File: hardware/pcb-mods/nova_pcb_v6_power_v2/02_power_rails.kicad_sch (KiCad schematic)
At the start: 12 parts, among them J12 XT30_JET_12V, J13 XT30_L2_12V, J2 UBEC_5V_AUX, U1 Pololu_D42V110F7_LEG_7V5, U2 Pololu_D42V110F12_HIP_12V, U3 Pololu_D24V22F12_L2_12V, U4 Pololu_D42V55F12_JET_12V, U5 Pololu_D42V55F7_ARM_7V5

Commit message: pcb(v6-power-v2): backfill MPN + Manufacturer fields — 100% BOM coverage
All 50 BOM components now carry MPNs from the verified order list:
Yageo RC0603 resistor set (R14 470k = Vishay CRCW0603 DigiKey sub),
Nichicon UPW1E bulk caps, Bourns SRR1260-220M, Infineon IRLB3034PBF,
onsemi BSS138 x3, TI LM393DR, Pololu buck modules (off-board),
GODIY INA226 20A R002 modules with I2C addresses in Manufacturer field,
AMASS XT60H/XT30U, JST B3B-XH-A, Adam Tech BHR-12-VUA, Sullins headers.
ERC: 0 errors (1 expected V7V5_ARM warning). kicad-happy bom_lock: pass.

Co-Authored-By: Claude Fable 5 <noreply@anthropic.com>
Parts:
- C6, C8, C9: MPN (none) -> UPW1E471MPD; Manufacturer (none) -> Nichicon
- J12, J13: MPN (none) -> XT30U-M; Manufacturer (none) -> AMASS
- J2: MPN (none) -> PRPC040SAAN-RC; Manufacturer (none) -> Sullins (snap to 1x03)
- L1: MPN (none) -> SRR1260-220M; Manufacturer (none) -> Bourns
- U1: MPN (none) -> D42V110F7; Manufacturer (none) -> Pololu (#5674, off-board module)
- U2: MPN (none) -> D42V110F12; Manufacturer (none) -> Pololu (#5677, off-board module)
- U3: MPN (none) -> D24V22F12; Manufacturer (none) -> Pololu (#2855, off-board module)
- U4: MPN (none) -> D42V55F12; Manufacturer (none) -> Pololu (#5577, off-board module)
- U5: MPN (none) -> D42V55F7; Manufacturer (none) -> Pololu (Phase 4 reserve, DNP)
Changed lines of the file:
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@@
+			)
+		)
+		(property "Manufacturer" "Pololu (#5577, off-board module)" (at 0 0 0)
+			(effects
+				(font
+					(size 1.27 1.27)
+				)
+				(hide yes)
+			)
+		)
+		(property "MPN" "D42V55F12" (at 0 0 0)
+			(effects
+				(font
+					(size 1.27 1.27)
+				)
+				(hide yes)
 			)
 		)
@@
 			)
 		)
+		(property "Manufacturer" "Sullins (snap to 1x03)" (at 0 0 0)
+			(effects
+				(font
+					(size 1.27 1.27)
+				)
+				(hide yes)
+			)
+		)
+		(property "MPN" "PRPC040SAAN-RC" (at 0 0 0)
+			(effects
+				(font
+					(size 1.27 1.27)
+				)
+				(hide yes)
+			)
+		)
 		(pin "1"
 		)
@@
 					(size 1.27 1.27)
 				)
+			)
+		)
+		(property "Manufacturer" "Pololu (#5674, off-board module)" (at 0 0 0)
+			(effects
+				(font
+					(size 1.27 1.27)
+				)
+				(hide yes)
+			)
+		)
+		(property "MPN" "D42V110F7" (at 0 0 0)
+			(effects
+				(font
+					(size 1.27 1.27)
+				)
+				(hide yes)
 			)
 		)
@@
 			)
 		)
+		(property "Manufacturer" "Pololu (Phase 4 reserve, DNP)" (at 0 0 0)
+			(effects
+				(font
+					(size 1.27 1.27)
+				)
+				(hide yes)
+			)
+		)
+		(property "MPN" "D42V55F7" (at 0 0 0)
+			(effects
+				(font
+					(size 1.27 1.27)
+				)
+				(hide yes)
+			)
+		)
 		(pin "1"
 		)
@@
 			)
 		)
+		(property "Manufacturer" "Pololu (#5677, off-board module)" (at 0 0 0)
+			(effects
+				(font
+					(size 1.27 1.27)
+				)
+				(hide yes)
+			)
+		)
+		(property "MPN" "D42V110F12" (at 0 0 0)
+			(effects
+				(font
+					(size 1.27 1.27)
+				)
+				(hide yes)
+			)
+		)
 		(pin "1"
 		)
@@
 			)
 		)
+		(property "Manufacturer" "Pololu (#2855, off-board module)" (at 0 0 0)
+			(effects
+				(font
+					(size 1.27 1.27)
+				)
+				(hide yes)
+			)
+		)
+		(property "MPN" "D24V22F12" (at 0 0 0)
+			(effects
+				(font
+					(size 1.27 1.27)
+				)
+				(hide yes)
+			)
+		)
 		(pin "1"
 		)
@@
 		(property "Datasheet" "~"
 			(at 129.54 105.41 0)
+			(effects
+				(font
+					(size 1.27 1.27)
+				)
+				(hide yes)
+			)
+		)
+		(property "Manufacturer" "AMASS" (at 0 0 0)
+			(effects
+				(font
+					(size 1.27 1.27)
+				)
+				(hide yes)
+			)
+		)
+		(property "MPN" "XT30U-M" (at 0 0 0)
 			(effects
 				(font
@@
 			)
 		)
+		(property "Manufacturer" "AMASS" (at 0 0 0)
+			(effects
+				(font
+					(size 1.27 1.27)
+				)
+				(hide yes)
+			)
+		)
+		(property "MPN" "XT30U-M" (at 0 0 0)
+			(effects
+				(font
+					(size 1.27 1.27)
+				)
+				(hide yes)
+			)
+		)
 		(pin "1"
 		)
@@
 			)
 		)
+		(property "Manufacturer" "Bourns" (at 0 0 0)
+			(effects
+				(font
+					(size 1.27 1.27)
+				)
+				(hide yes)
+			)
+		)
+		(property "MPN" "SRR1260-220M" (at 0 0 0)
+			(effects
+				(font
+					(size 1.27 1.27)
+				)
+				(hide yes)
+			)
+		)
 		(pin "1"
 		)
@@
 			)
 		)
+		(property "Manufacturer" "Nichicon" (at 0 0 0)
+			(effects
+				(font
+					(size 1.27 1.27)
+				)
+				(hide yes)
+			)
+		)
+		(property "MPN" "UPW1E471MPD" (at 0 0 0)
+			(effects
+				(font
+					(size 1.27 1.27)
+				)
+				(hide yes)
+			)
+		)
 		(pin "1"
 		)
@@
 			)
 		)
+		(property "Manufacturer" "Nichicon" (at 0 0 0)
+			(effects
+				(font
+					(size 1.27 1.27)
+				)
+				(hide yes)
+			)
+		)
+		(property "MPN" "UPW1E471MPD" (at 0 0 0)
+			(effects
+				(font
+					(size 1.27 1.27)
+				)
+				(hide yes)
+			)
+		)
 		(pin "1"
 		)
@@
 			(effects
 				(font
+					(size 1.27 1.27)
+				)
+				(hide yes)
+			)
+		)
+		(property "Manufacturer" "Nichicon" (at 0 0 0)
+			(effects
+				(font
+					(size 1.27 1.27)
+				)
+				(hide yes)
+			)
+		)
+		(property "MPN" "UPW1E471MPD" (at 0 0 0)
+			(effects
+				(font

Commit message: pcb(v6-power-v2): correct C1-C5 to FymuSing (as purchased) + DigiKey PNs from order CSV
Verified against Complete_Digikey_Order_NOVA.csv (16 lines, all match):
R14 470k confirmed Vishay CRCW0603470KFKEA (541-470KHCT-ND).
C1-C5 corrected Nichicon->FymuSing 1000uF/25V (Amazon purchase, 10x17mm).
Remaining 23 parts without DigiKey PN are Amazon/Pololu/AMASS sourced.

Co-Authored-By: Claude Fable 5 <noreply@anthropic.com>
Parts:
- C6, C8, C9: DigiKey (none) -> 493-1826-ND
- J2: DigiKey (none) -> S1011EC-40-ND
- L1: DigiKey (none) -> SRR1260-220MCT-ND
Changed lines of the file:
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@@
+			)
+		)
+		(property "DigiKey" "S1011EC-40-ND" (at 0 0 0)
+			(effects
+				(font
+					(size 1.27 1.27)
+				)
+				(hide yes)
 			)
 		)
@@
 			)
 		)
+		(property "DigiKey" "SRR1260-220MCT-ND" (at 0 0 0)
+			(effects
+				(font
+					(size 1.27 1.27)
+				)
+				(hide yes)
+			)
+		)
 		(pin "1"
 		)
@@
 			)
 		)
+		(property "DigiKey" "493-1826-ND" (at 0 0 0)
+			(effects
+				(font
+					(size 1.27 1.27)
+				)
+				(hide yes)
+			)
+		)
 		(pin "1"
 		)
@@
 			)
 		)
+		(property "DigiKey" "493-1826-ND" (at 0 0 0)
+			(effects
+				(font
+					(size 1.27 1.27)
+				)
+				(hide yes)
+			)
+		)
 		(pin "1"
 		)
@@
 			(effects
 				(font
+					(size 1.27 1.27)
+				)
+				(hide yes)
+			)
+		)
+		(property "DigiKey" "493-1826-ND" (at 0 0 0)
+			(effects
+				(font

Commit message: pcb(v6-power-v2): AssemblyOrder fields + assembly-sequenced iBOM
15-step hand-solder sequence (flat->tall, SMD bottom cluster -> THT top):
0603s -> SOT-23 -> SOIC -> L1 -> INA headers -> headers/JST/IDC ->
screw blocks -> XT30 -> XT60 -> Q1 (Step 10a test first) -> 470uF -> 1000uF.
bom/ibom_assembly.html groups by AssemblyOrder via netlist extra-data.

Co-Authored-By: Claude Fable 5 <noreply@anthropic.com>
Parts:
- C6, C8, C9: AssemblyOrder (none) -> 14 THT 470uF
- J12, J13: AssemblyOrder (none) -> 11 THT XT30
- J2: AssemblyOrder (none) -> 07 THT pin header
- L1: AssemblyOrder (none) -> 05 SMD inductor (big pads, max iron heat)
- U1, U2, U3, U4: AssemblyOrder (none) -> 11 THT XT30 (buck landing)
- U5: AssemblyOrder (none) -> 11 THT XT30 (buck landing, DNP option)
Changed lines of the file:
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@@
+			)
+		)
+		(property "AssemblyOrder" "11 THT XT30 (buck landing)" (at 0 0 0)
+			(effects
+				(font
+					(size 1.27 1.27)
+				)
+				(hide yes)
 			)
 		)
@@
 			)
 		)
+		(property "AssemblyOrder" "07 THT pin header" (at 0 0 0)
+			(effects
+				(font
+					(size 1.27 1.27)
+				)
+				(hide yes)
+			)
+		)
 		(pin "1"
 		)
@@
 		)
 		(property "MPN" "D42V110F7" (at 0 0 0)
+			(effects
+				(font
+					(size 1.27 1.27)
+				)
+				(hide yes)
+			)
+		)
+		(property "AssemblyOrder" "11 THT XT30 (buck landing)" (at 0 0 0)
 			(effects
 				(font
@@
 			)
 		)
+		(property "AssemblyOrder" "11 THT XT30 (buck landing, DNP option)" (at 0 0 0)
+			(effects
+				(font
+					(size 1.27 1.27)
+				)
+				(hide yes)
+			)
+		)
 		(pin "1"
 		)
@@
 			)
 		)
+		(property "AssemblyOrder" "11 THT XT30 (buck landing)" (at 0 0 0)
+			(effects
+				(font
+					(size 1.27 1.27)
+				)
+				(hide yes)
+			)
+		)
 		(pin "1"
 		)
@@
 			)
 		)
+		(property "AssemblyOrder" "11 THT XT30 (buck landing)" (at 0 0 0)
+			(effects
+				(font
+					(size 1.27 1.27)
+				)
+				(hide yes)
+			)
+		)
 		(pin "1"
 		)
@@
 		)
 		(property "MPN" "XT30U-M" (at 0 0 0)
+			(effects
+				(font
+					(size 1.27 1.27)
+				)
+				(hide yes)
+			)
+		)
+		(property "AssemblyOrder" "11 THT XT30" (at 0 0 0)
 			(effects
 				(font
@@
 			)
 		)
+		(property "AssemblyOrder" "11 THT XT30" (at 0 0 0)
+			(effects
+				(font
+					(size 1.27 1.27)
+				)
+				(hide yes)
+			)
+		)
 		(pin "1"
 		)
@@
 			)
 		)
+		(property "AssemblyOrder" "05 SMD inductor (big pads, max iron heat)" (at 0 0 0)
+			(effects
+				(font
+					(size 1.27 1.27)
+				)
+				(hide yes)
+			)
+		)
 		(pin "1"
 		)
@@
 			)
 		)
+		(property "AssemblyOrder" "14 THT 470uF" (at 0 0 0)
+			(effects
+				(font
+					(size 1.27 1.27)
+				)
+				(hide yes)
+			)
+		)
 		(pin "1"
 		)
@@
 			)
 		)
+		(property "AssemblyOrder" "14 THT 470uF" (at 0 0 0)
+			(effects
+				(font
+					(size 1.27 1.27)
+				)
+				(hide yes)
+			)
+		)
 		(pin "1"
 		)
@@
 			(effects
 				(font
+					(size 1.27 1.27)
+				)
+				(hide yes)
+			)
+		)
+		(property "AssemblyOrder" "14 THT 470uF" (at 0 0 0)
+			(effects
+				(font

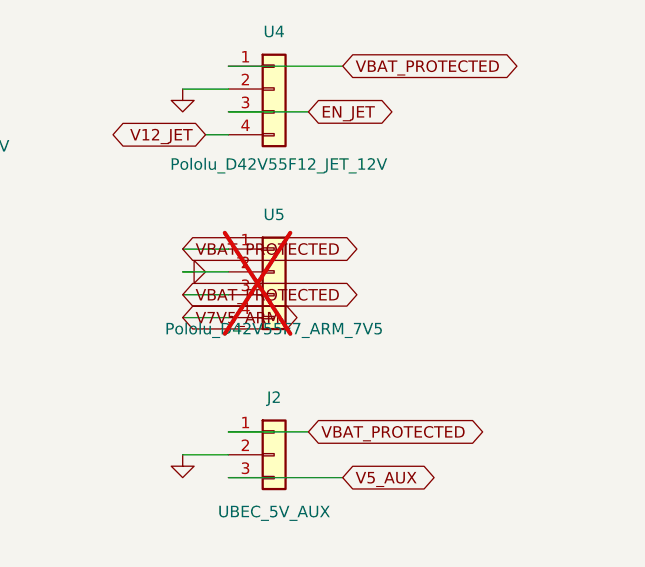
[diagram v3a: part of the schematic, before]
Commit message: power board: arm Phase-4 schematic edits (EN re-gate + J14 + arm INA226) + README status
Commits the ERC-clean (0/0) arm Phase-4 schematic work that had been uncommitted
all session (and nearly lost to a stray stash):
- 02_power_rails: U5.EN re-gated VBAT_PROTECTED->EN_BUCKS (arm buck now under the
  same E-stop/undervoltage chain as legs); J14 arm-output XT30 (fixes the former
  dangling V7V5_ARM single-pad net).
- 06_safety_chain: U12 arm-rail INA226 (addr 0x45, DNP Phase-4) + no-connects.
- README status line refreshed to match reality + point at STATUS.md.

The .kicad_pcb is intentionally NOT included — those footprints are F8'd but
still need GUI placement + routing (tracked as blocker B1 in STATUS.md).

Co-Authored-By: Claude Opus 4.8 <noreply@anthropic.com>
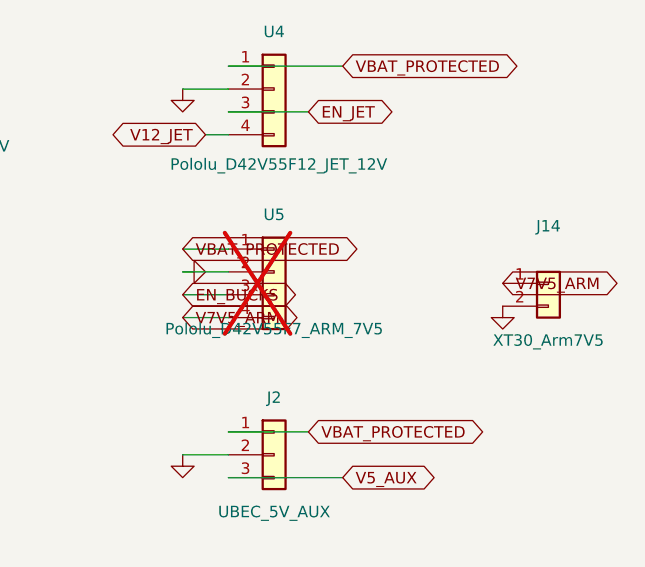
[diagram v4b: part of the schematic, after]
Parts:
- added J14: XT30_Arm7V5, Connector_AMASS:AMASS_XT30U-M_1x02_P5.0mm_Vertical, symbol Connector_Generic:Conn_01x02
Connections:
- net EN_BUCKS: now also U5.3 (Pin_3)
- net GND: now also J14.2 (Pin_2)
- net V7V5_ARM: now also J14.1 (Pin_1)
- net VBAT_PROTECTED: no longer U5.3 (Pin_3)
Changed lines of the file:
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@@
 		)
 	)
-	(global_label "VBAT_PROTECTED"
+	(global_label "EN_BUCKS"
 		(shape bidirectional)
 		(at 154.94 128.27 0)
@@
 					(unit 1)
 				)
+			)
+		)
+	)
+	(symbol
+		(lib_id "Connector_Generic:Conn_01x02")
+		(at 195.58 127 0)
+		(unit 1)
+		(exclude_from_sim no)
+		(in_bom yes)
+		(on_board yes)
+		(dnp no)
+		(property "Reference" "J14"
+			(at 195.58 120.65 0)
+			(effects
+				(font
+					(size 1.27 1.27)
+				)
+			)
+		)
+		(property "Value" "XT30_Arm7V5"
+			(at 195.58 133.35 0)
+			(effects
+				(font
+					(size 1.27 1.27)
+				)
+			)
+		)
+		(property "Footprint" "Connector_AMASS:AMASS_XT30U-M_1x02_P5.0mm_Vertical"
+			(at 195.58 127 0)
+			(effects
+				(font
+					(size 1.27 1.27)
+				)
+				(hide yes)
+			)
+		)
+		(property "Datasheet" "~"
+			(at 195.58 127 0)
+			(effects
+				(font
+					(size 1.27 1.27)
+				)
+				(hide yes)
+			)
+		)
+		(property "Description" ""
+			(at 195.58 127 0)
+			(effects
+				(font
+					(size 1.27 1.27)
+				)
+			)
+		)
+		(property "Manufacturer" "AMASS" (at 0 0 0)
+			(effects
+				(font
+					(size 1.27 1.27)
+				)
+				(hide yes)
+			)
+		)
+		(property "MPN" "XT30U-M" (at 0 0 0)
+			(effects
+				(font
+					(size 1.27 1.27)
+				)
+				(hide yes)
+			)
+		)
+		(property "AssemblyOrder" "11 THT XT30" (at 0 0 0)
+			(effects
+				(font
+					(size 1.27 1.27)
+				)
+				(hide yes)
+			)
+		)
+		(pin "1"
+		)
+		(pin "2"
+		)
+		(instances
+			(project "nova_pcb_v6_power_v2"
+				(path "/f535083b-f621-4317-a378-cf746e7f972b/27a07a1d-f9e1-432b-b0b9-19fa0d701a09"
+					(reference "J14")
+					(unit 1)
+				)
+			)
+		)
+	)
+	(global_label "V7V5_ARM"
+		(shape bidirectional)
+		(at 190.5 127 0)
+		(effects
+			(font
+				(size 1.27 1.27)
+			)
+			(justify left)
+		)
+		(property "Intersheetrefs" "${INTERSHEET_REFS}"
+			(at 190.5 127 0)
+			(effects
+				(font
+					(size 1.27 1.27)
+				)
+				(hide yes)
+			)
+		)
+	)
+	(symbol
+		(lib_id "power:GND")
+		(at 190.5 129.54 0)
+		(unit 1)
+		(exclude_from_sim no)
+		(in_bom yes)
+		(on_board yes)
+		(dnp no)
+		(property "Reference" "#PWR218"
+			(at 196.85 129.54 270)
+			(effects
+				(font
+					(size 1.27 1.27)
+				)
+				(hide yes)
+			)
+		)
+		(property "Value" "GND"
+			(at 184.15 129.54 270)
+			(effects
+				(font
+					(size 1.27 1.27)
+				)
+				(hide yes)
+			)
+		)
+		(property "Footprint" ""
+			(at 190.5 129.54 0)
+			(effects
+				(font
+					(size 1.27 1.27)
+				)
+				(hide yes)
+			)
+		)
+		(property "Datasheet" "~"
+			(at 190.5 129.54 0)
+			(effects
+				(font
+					(size 1.27 1.27)
+				)
+				(hide yes)
+			)
+		)
+		(property "Description" ""
+			(at 190.5 129.54 0)
+			(effects
+				(font
+					(size 1.27 1.27)
+				)
+			)
+		)
+		(pin "1"
+		)
+		(instances
+			(project "nova_pcb_v6_power_v2"
+				(path "/f535083b-f621-4317-a378-cf746e7f972b/27a07a1d-f9e1-432b-b0b9-19fa0d701a09"
+					(reference "#PWR218")
+					(unit 1)
+				)

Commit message: power board: fix reversed XT connector polarity (all 9 AMASS XT)
AMASS XT footprints number pad1=chamfer/NEGATIVE, pad2=flat/POSITIVE.
Board had +V wired to pad1 -> every keyed power connector reverse-wired:
J1 (XT60 battery in), J3-J7 (rail injection), J12-J14 (Jetson/L2/arm out).
Mating a normally-built cable would feed +V to the - terminal and fry the
connected load (Jetson, servos, arm). Confirmed against footprint flat/chamfer
geometry + physical connector (flat=+).

Fix: swapped pin1/pin2 net assignment on all 9 connectors in schematic,
re-routed PCB, regenerated 14-file gerber set. Pololu bucks use a custom
non-keyed terminal (pad1=rect=+V) and were correctly left unchanged.

Verify: ERC 0, DRC 0 hard / 0 unconnected, fab_gate GO, J20 match intact.

Co-Authored-By: Claude Opus 4.8 <noreply@anthropic.com>
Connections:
- net GND: now also J12.1 (Pin_1), J13.1 (Pin_1), J14.1 (Pin_1); no longer J12.2 (Pin_2), J13.2 (Pin_2), J14.2 (Pin_2)
- net V12_JET: now also J12.2 (Pin_2); no longer J12.1 (Pin_1)
- net V12_L2: now also J13.2 (Pin_2); no longer J13.1 (Pin_1)
- net V7V5_ARM: now also J14.2 (Pin_2); no longer J14.1 (Pin_1)
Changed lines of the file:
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@@
 	(wire
 		(pts
-			(xy 124.46 105.41) (xy 119.38 105.41)
-		)
-		(stroke
-			(width 0)
-			(type default)
-		)
-	)
-	(wire
-		(pts
 			(xy 88.9 148.59) (xy 88.9 143.51)
 		)
@@
 	(wire
 		(pts
-			(xy 160.02 128.27) (xy 154.94 128.27)
+			(xy 119.38 85.09) (xy 124.46 85.09)
 		)
 		(stroke
@@
 	(wire
 		(pts
-			(xy 160.02 146.05) (xy 154.94 146.05)
+			(xy 160.02 128.27) (xy 154.94 128.27)
 		)
 		(stroke
@@
 	(wire
 		(pts
-			(xy 107.95 156.21) (xy 107.95 161.29)
+			(xy 160.02 146.05) (xy 154.94 146.05)
 		)
 		(stroke
@@
 	(wire
 		(pts
-			(xy 124.46 87.63) (xy 119.38 87.63)
+			(xy 119.38 87.63) (xy 124.46 87.63)
 		)
 		(stroke
@@
 	(wire
 		(pts
-			(xy 57.15 148.59) (xy 57.15 146.05)
+			(xy 107.95 156.21) (xy 107.95 161.29)
 		)
 		(stroke
@@
 	(wire
 		(pts
-			(xy 160.02 130.81) (xy 154.94 130.81)
+			(xy 57.15 148.59) (xy 57.15 146.05)
 		)
 		(stroke
@@
 	(wire
 		(pts
-			(xy 124.46 107.95) (xy 119.38 107.95)
+			(xy 160.02 130.81) (xy 154.94 130.81)
 		)
 		(stroke
@@
 	(wire
 		(pts
-			(xy 124.46 85.09) (xy 119.38 85.09)
+			(xy 119.38 107.95) (xy 124.46 107.95)
 		)
 		(stroke
@@
 	(wire
 		(pts
-			(xy 160.02 148.59) (xy 172.72 148.59)
+			(xy 160.02 148.59) (xy 146.05 148.59)
 		)
 		(stroke
@@
 	(wire
 		(pts
+			(xy 119.38 105.41) (xy 124.46 105.41)
+		)
+		(stroke
+			(width 0)
+			(type default)
+		)
+	)
+	(wire
+		(pts
 			(xy 88.9 156.21) (xy 88.9 161.29)
 		)
@@
 	(wire
 		(pts
-			(xy 160.02 143.51) (xy 168.91 143.51)
+			(xy 160.02 143.51) (xy 151.13 143.51)
 		)
 		(stroke
@@
 	(global_label "V12_L2"
 		(shape bidirectional)
-		(at 119.38 85.09 0)
+		(at 119.38 87.63 180)
 		(effects
 			(font
 				(size 1.27 1.27)
 			)
-			(justify left)
+			(justify right)
 		)
 		(property "Intersheetrefs" "${INTERSHEET_REFS}"
-			(at 119.38 85.09 0)
+			(at 119.38 87.63 0)
 			(effects
 				(font
@@
 	(global_label "V7V5_ARM"
 		(shape bidirectional)
-		(at 190.5 127 0)
+		(at 190.5 129.54 180)
 		(effects
 			(font
 				(size 1.27 1.27)
 			)
-			(justify left)
+			(justify right)
 		)
 		(property "Intersheetrefs" "${INTERSHEET_REFS}"
-			(at 190.5 127 0)
+			(at 190.5 129.54 0)
 			(effects
 				(font
@@
 	(global_label "V5_AUX"
 		(shape bidirectional)
-		(at 172.72 148.59 0)
+		(at 146.05 148.59 180)
 		(effects
 			(font
 				(size 1.27 1.27)
 			)
-			(justify left)
+			(justify right)
 		)
 		(property "Intersheetrefs" "${INTERSHEET_REFS}"
-			(at 172.72 148.59 0)
+			(at 146.05 148.59 0)
 			(effects
 				(font
@@
 	(global_label "VBAT_PROTECTED"
 		(shape bidirectional)
-		(at 168.91 143.51 0)
+		(at 151.13 143.51 180)
 		(effects
 			(font
 				(size 1.27 1.27)
 			)
-			(justify left)
+			(justify right)
 		)
 		(property "Intersheetrefs" "${INTERSHEET_REFS}"
-			(at 168.91 143.51 0)
+			(at 151.13 143.51 0)
 			(effects
 				(font
@@
 	(global_label "V12_JET"
 		(shape bidirectional)
-		(at 119.38 105.41 0)
+		(at 119.38 107.95 180)
 		(effects
 			(font
 				(size 1.27 1.27)
 			)
-			(justify left)
+			(justify right)
 		)
 		(property "Intersheetrefs" "${INTERSHEET_REFS}"
-			(at 119.38 105.41 0)
+			(at 119.38 107.95 0)
 			(effects
 				(font
@@
 	(symbol
 		(lib_id "power:GND")
-		(at 154.94 146.05 0)
+		(at 154.94 146.05 270)
 		(unit 1)
 		(exclude_from_sim no)
@@
 		(dnp no)
 		(property "Reference" "#PWR26"
-			(at 161.29 146.05 270)
+			(at 154.94 152.4 270)
 			(effects
 				(font
@@
 		)
 		(property "Value" "GND"
-			(at 148.59 146.05 270)
+			(at 154.94 139.7 270)
 			(effects
 				(font
@@
 	(symbol
 		(lib_id "power:GND")
-		(at 119.38 87.63 90)
+		(at 119.38 85.09 180)
 		(unit 1)
 		(exclude_from_sim no)
@@
 		(dnp no)
 		(property "Reference" "#PWR28"
-			(at 119.38 81.28 270)
+			(at 113.03 85.09 270)
 			(effects
 				(font
@@
 		)
 		(property "Value" "GND"
-			(at 119.38 93.98 270)
+			(at 125.73 85.09 270)
 			(effects
 				(font
@@
 		)
 		(property "Footprint" ""
-			(at 119.38 87.63 0)
+			(at 119.38 85.09 0)
 			(effects
 				(font
@@
 		)
 		(property "Datasheet" "~"
-			(at 119.38 87.63 0)
+			(at 119.38 85.09 0)
 			(effects
 				(font
@@
 		)
 		(property "Description" ""
-			(at 119.38 87.63 0)
+			(at 119.38 85.09 0)
 			(effects
 				(font
@@
 	(symbol
 		(lib_id "power:GND")
-		(at 119.38 107.95 90)
+		(at 119.38 105.41 180)
 		(unit 1)
 		(exclude_from_sim no)
@@
 		(dnp no)
 		(property "Reference" "#PWR27"
-			(at 119.38 101.6 270)
+			(at 113.03 105.41 270)
 			(effects
 				(font
@@
 		)
 		(property "Value" "GND"
-			(at 119.38 114.3 270)
+			(at 125.73 105.41 270)
 			(effects
 				(font
@@
 		)
 		(property "Footprint" ""
-			(at 119.38 107.95 0)
+			(at 119.38 105.41 0)
 			(effects
 				(font
@@
 		)
 		(property "Datasheet" "~"
-			(at 119.38 107.95 0)
+			(at 119.38 105.41 0)
 			(effects
 				(font
@@
 		)
 		(property "Description" ""
-			(at 119.38 107.95 0)
+			(at 119.38 105.41 0)
 			(effects
 				(font
@@
 	(symbol
 		(lib_id "power:GND")
-		(at 190.5 129.54 0)
+		(at 190.5 127 180)
 		(unit 1)
 		(exclude_from_sim no)
@@
 		(dnp no)
 		(property "Reference" "#PWR218"
-			(at 196.85 129.54 270)
+			(at 184.15 127 270)
 			(effects
 				(font
@@
 		)
 		(property "Value" "GND"
-			(at 184.15 129.54 270)
+			(at 196.85 127 270)
 			(effects
 				(font
@@
 		)
 		(property "Footprint" ""
-			(at 190.5 129.54 0)
+			(at 190.5 127 0)
 			(effects
 				(font
@@
 		)
 		(property "Datasheet" "~"
-			(at 190.5 129.54 0)
+			(at 190.5 127 0)
 			(effects
 				(font
@@
 		)
 		(property "Description" ""
-			(at 190.5 129.54 0)
+			(at 190.5 127 0)
 			(effects
 				(font
